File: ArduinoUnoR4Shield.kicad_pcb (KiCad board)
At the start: 2 copper layers, 68.6 x 53.3 mm, 11 parts, among them U1 OFF, U2 Analog_1, U3 Analog_2, U4 ESP32-S3, U5 ICSP, U6 Digital_1, U7 Digital_2

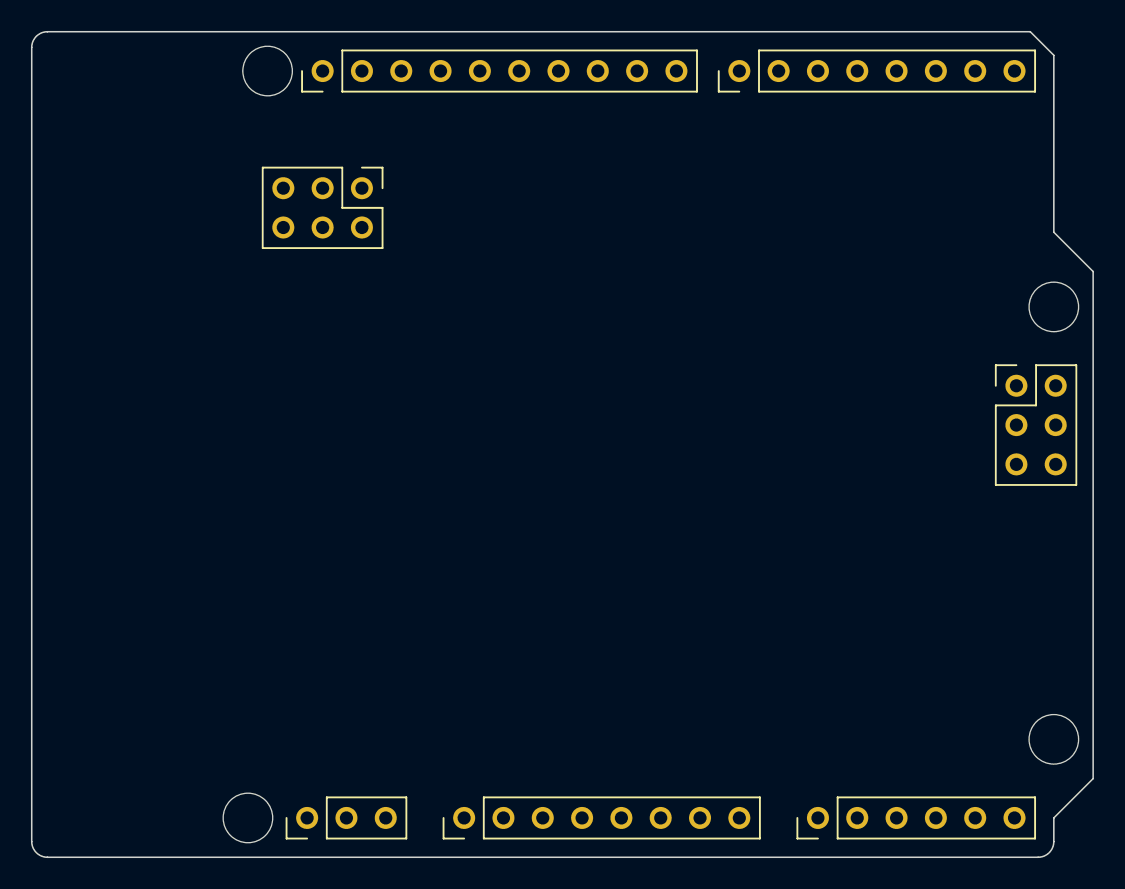
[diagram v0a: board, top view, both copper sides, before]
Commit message: Added Proto Design
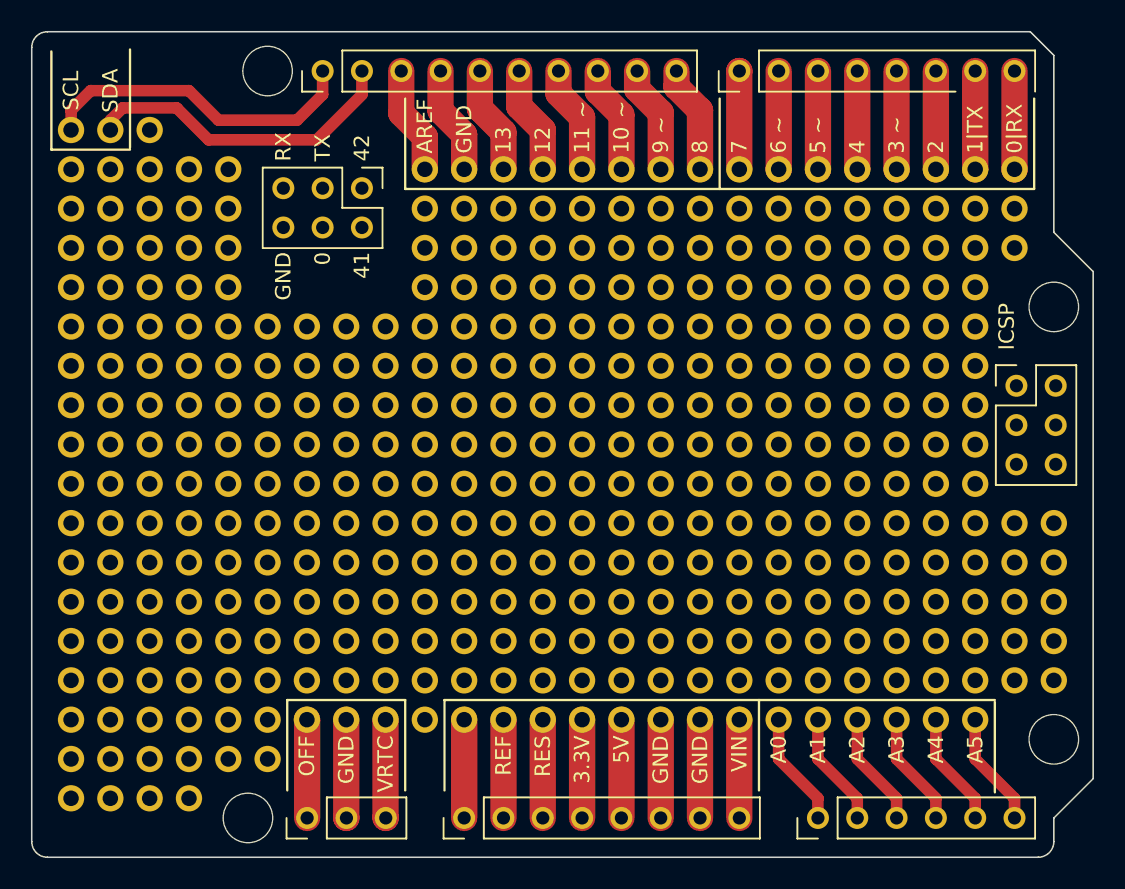
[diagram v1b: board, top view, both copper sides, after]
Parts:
- added REF**: PinSocket_1x24_P2.54mm_Vertical, Connector_PinSocket_2.54mm:PinSocket_1x24_P2.54mm_Vertical, F.Cu at (109.2, 90.2)
- added REF**: PinSocket_1x24_P2.54mm_Vertical, Connector_PinSocket_2.54mm:PinSocket_1x24_P2.54mm_Vertical, F.Cu at (109.2, 87.6)
- added REF**: PinSocket_1x24_P2.54mm_Vertical, Connector_PinSocket_2.54mm:PinSocket_1x24_P2.54mm_Vertical, F.Cu at (109.2, 92.7)
- added REF**: PinSocket_1x24_P2.54mm_Vertical, Connector_PinSocket_2.54mm:PinSocket_1x24_P2.54mm_Vertical, F.Cu at (109.2, 72.4)
- added REF**: PinSocket_1x24_P2.54mm_Vertical, Connector_PinSocket_2.54mm:PinSocket_1x24_P2.54mm_Vertical, F.Cu at (109.2, 110.5)
- added REF**: PinSocket_1x24_P2.54mm_Vertical, Connector_PinSocket_2.54mm:PinSocket_1x24_P2.54mm_Vertical, F.Cu at (109.2, 108.0)
- added REF**: PinSocket_1x24_P2.54mm_Vertical, Connector_PinSocket_2.54mm:PinSocket_1x24_P2.54mm_Vertical, F.Cu at (109.2, 95.2)
- added REF**: PinSocket_1x24_P2.54mm_Vertical, Connector_PinSocket_2.54mm:PinSocket_1x24_P2.54mm_Vertical, F.Cu at (109.2, 80.0)
- added REF**: PinSocket_1x24_P2.54mm_Vertical, Connector_PinSocket_2.54mm:PinSocket_1x24_P2.54mm_Vertical, F.Cu at (109.2, 74.9)
- added REF**: PinSocket_1x24_P2.54mm_Vertical, Connector_PinSocket_2.54mm:PinSocket_1x24_P2.54mm_Vertical, F.Cu at (109.2, 82.5)
- added REF**: PinSocket_1x24_P2.54mm_Vertical, Connector_PinSocket_2.54mm:PinSocket_1x24_P2.54mm_Vertical, F.Cu at (109.2, 97.8)
- added REF**: PinSocket_1x24_P2.54mm_Vertical, Connector_PinSocket_2.54mm:PinSocket_1x24_P2.54mm_Vertical, F.Cu at (109.2, 77.5)
- added REF**: PinSocket_1x24_P2.54mm_Vertical, Connector_PinSocket_2.54mm:PinSocket_1x24_P2.54mm_Vertical, F.Cu at (109.2, 85.1)
- added REF**: PinSocket_1x24_P2.54mm_Vertical, Connector_PinSocket_2.54mm:PinSocket_1x24_P2.54mm_Vertical, F.Cu at (109.2, 102.9)
- added REF**: PinSocket_1x24_P2.54mm_Vertical, Connector_PinSocket_2.54mm:PinSocket_1x24_P2.54mm_Vertical, F.Cu at (109.2, 113.0)
- added REF**: PinSocket_1x24_P2.54mm_Vertical, Connector_PinSocket_2.54mm:PinSocket_1x24_P2.54mm_Vertical, F.Cu at (109.2, 115.6)
- added REF**: PinSocket_1x24_P2.54mm_Vertical, Connector_PinSocket_2.54mm:PinSocket_1x24_P2.54mm_Vertical, F.Cu at (109.2, 100.3)
- added REF**: PinSocket_1x24_P2.54mm_Vertical, Connector_PinSocket_2.54mm:PinSocket_1x24_P2.54mm_Vertical, F.Cu at (109.2, 105.4)
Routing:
- net unconnected-(U6-Pad2): track 0.00 -> 21.1 mm
- net unconnected-(U6-Pad1): track 0.00 -> 21.0 mm
- net unconnected-(U3-Pad14): track 0.00 -> 7.40 mm
- net unconnected-(U3-Pad10): track 0.00 -> 7.40 mm
- net unconnected-(U3-Pad9): track 0.00 -> 7.40 mm
- net unconnected-(U3-Pad13): track 0.00 -> 7.40 mm
- net unconnected-(U3-Pad12): track 0.00 -> 7.40 mm
- net unconnected-(U3-Pad11): track 0.00 -> 7.40 mm
- net unconnected-(U6-Pad9): track 0.00 -> 6.98 mm
- net unconnected-(U6-Pad8): track 0.00 -> 6.98 mm
- net unconnected-(U6-Pad7): track 0.00 -> 6.98 mm
- net unconnected-(U6-Pad6): track 0.00 -> 6.98 mm
- net unconnected-(U6-Pad5): track 0.00 -> 6.98 mm
- net unconnected-(U6-Pad4): track 0.00 -> 6.98 mm
- net unconnected-(U6-Pad3): track 0.00 -> 6.98 mm
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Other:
- board text added: "0"
- board text added: "0|RX"
- board text added: "10"
- board text added: "11"
- board text added: "12"
- board text added: "13"
- board text added: "1|TX"
- board text added: "2"
- board text added: "3"
- board text added: "3.3V"
- board text added: "4"
- board text added: "41"
- board text added: "42"
- board text added: "5"
- board text added: "5V"
- board text added: "6"
- board text added: "7"
- board text added: "8"
- board text added: "9"
- board text added: "A0"
- board text added: "A1"
- board text added: "A2"
- board text added: "A3"
- board text added: "A4"
- board text added: "A5"
- board text added: "AREF"
- board text added: "GND"
- board text added: "ICSP"
- board text added: "OFF"
- board text added: "REF"
- board text added: "RES"
- board text added: "RX"
- board text added: "SCL"
- board text added: "SDA"
- board text added: "TX"
- board text added: "VIN"
- board text added: "VRTC"
- board text added: "~"
